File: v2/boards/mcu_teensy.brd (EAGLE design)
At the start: 27.6 x 72.2 mm, 9 parts, among them Q1 BS108, U1 TEENSY3_6, U2 MCP101

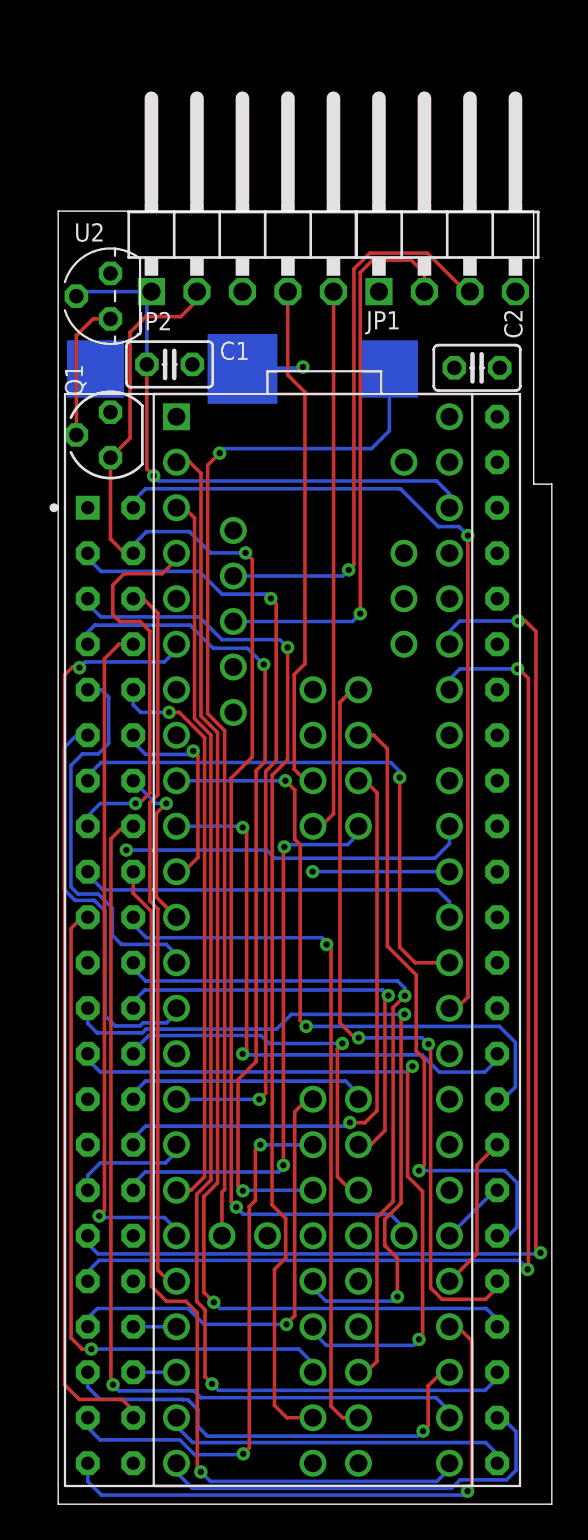
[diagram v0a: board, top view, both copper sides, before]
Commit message: ct-Bot v2 prototype test boards updated/added
Simplified mainboard, teensy mcu board, and sensor boards are very early prototypes just for development and testing.
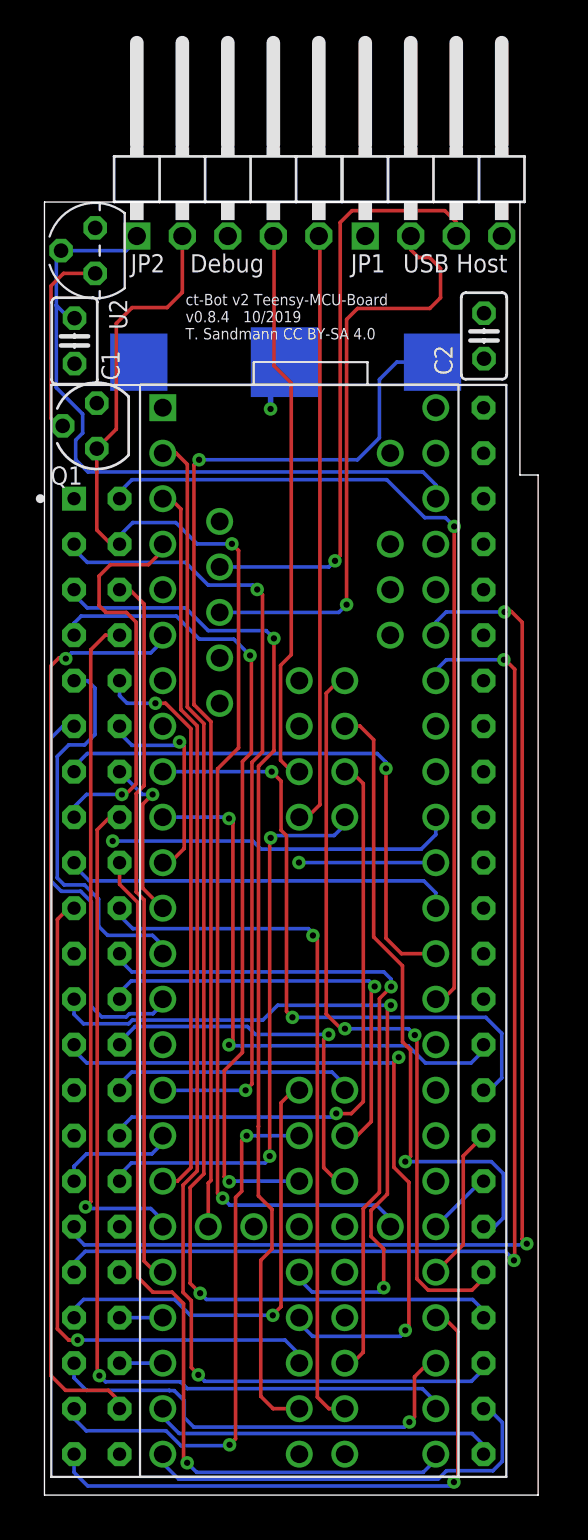
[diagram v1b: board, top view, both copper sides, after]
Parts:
- moved C1 5.47 mm to (1.67, 64.4), turned to 270 degrees
- moved JP2 3.21 mm to (10.2, 74.1)
- moved JP1 3.20 mm to (21.7, 74.1)
- moved U2 2.68 mm to (2.83, 69.5)
- moved BAT1 2.44 mm to (13.5, 63.2)
- moved C2 1.82 mm to (24.5, 64.7), turned to 90 degrees
- moved U1 0.92 mm to (14.2, 31.5)
- moved Q1 0.92 mm to (2.92, 59.7)
- moved ST1 0.92 mm to (13.1, 30.2)
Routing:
- net +5V: track 32.6 -> 40.8 mm
- net 3V3_TEENSY: track 32.5 -> 40.0 mm, vias 1 -> 0
- net N$1: track 7.84 -> 11.0 mm
- net VBAT_RTC: track 57.9 -> 60.6 mm
- net SWDIO: track 30.6 -> 33.2 mm
- net SWDCLK: track 28.6 -> 31.2 mm
- net RESET: track 73.7 -> 76.2 mm
- net USB1_D_N: track 31.2 -> 33.4 mm
- net USB1_D_P: track 31.5 -> 33.4 mm
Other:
- board text added: "Debug"
- board text added: "USB Host"
- board text added: "ct-Bot v2 Teensy-MCU-Board v0.8.4 10/2019 T. Sandmann CC BY-SA 4.0"
